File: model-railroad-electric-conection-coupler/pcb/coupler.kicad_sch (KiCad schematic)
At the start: 3 parts, among them J1 Conn_01x03_Pin, J2 Conn_01x06_Pin, J3 Conn_01x03_Pin

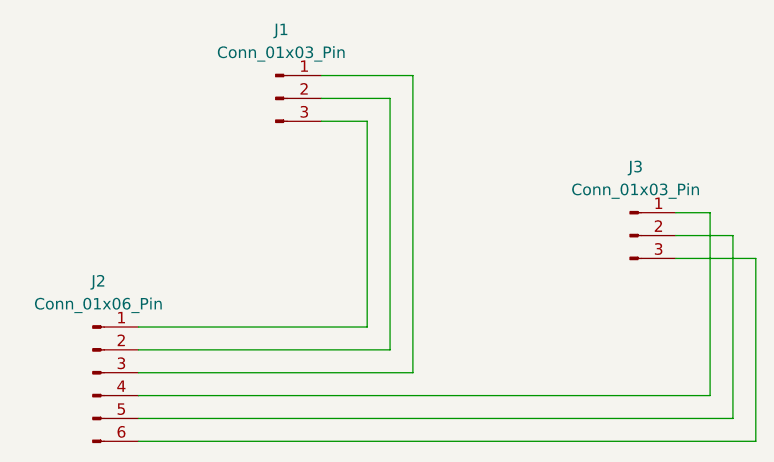
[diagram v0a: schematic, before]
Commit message: 鉄道模型用の通電カプラー PCB 版 v1
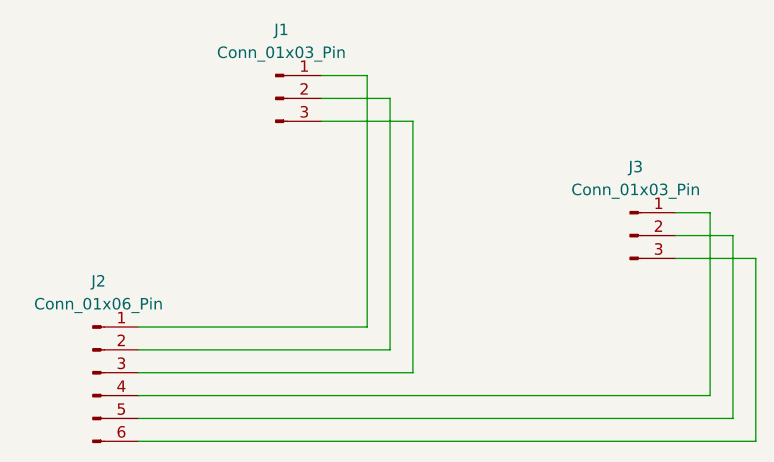
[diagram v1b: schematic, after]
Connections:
- net at J2.1 (Pin_1): now also J1.1 (Pin_1); no longer J1.3 (Pin_3)
- net at J2.3 (Pin_3): now also J1.3 (Pin_3); no longer J1.1 (Pin_1)
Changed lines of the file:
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@@
 	(wire
 		(pts
-			(xy 80.01 73.66) (xy 85.09 73.66)
+			(xy 85.09 96.52) (xy 85.09 68.58)
 		)
 		(stroke
@@
 	(wire
 		(pts
-			(xy 80.01 68.58) (xy 90.17 68.58)
+			(xy 85.09 68.58) (xy 80.01 68.58)
+		)
+		(stroke
+			(width 0)
+			(type default)
+		)
+	)
+	(wire
+		(pts
+			(xy 128.27 109.22) (xy 59.69 109.22)
+		)
+		(stroke
+			(width 0)
+			(type default)
+		)
+	)
+	(wire
+		(pts
+			(xy 87.63 71.12) (xy 87.63 99.06)
+		)
+		(stroke
+			(width 0)
+			(type default)
+		)
+	)
+	(wire
+		(pts
+			(xy 123.19 83.82) (xy 123.19 104.14)
+		)
+		(stroke
+			(width 0)
+			(type default)
+		)
+	)
+	(wire
+		(pts
+			(xy 90.17 73.66) (xy 90.17 101.6)
+		)
+		(stroke
+			(width 0)
+			(type default)
+		)
+	)
+	(wire
+		(pts
+			(xy 128.27 88.9) (xy 128.27 109.22)
 		)
 		(stroke
@@
 	(wire
 		(pts
-			(xy 128.27 109.22) (xy 59.69 109.22)
+			(xy 119.38 83.82) (xy 123.19 83.82)
 		)
 		(stroke
@@
 	(wire
 		(pts
-			(xy 123.19 83.82) (xy 123.19 104.14)
-		)
-		(stroke
-			(width 0)
-			(type default)
-		)
-	)
-	(wire
-		(pts
-			(xy 128.27 88.9) (xy 128.27 109.22)
-		)
-		(stroke
-			(width 0)
-			(type default)
-		)
-	)
-	(wire
-		(pts
-			(xy 90.17 68.58) (xy 90.17 101.6)
-		)
-		(stroke
-			(width 0)
-			(type default)
-		)
-	)
-	(wire
-		(pts
-			(xy 87.63 71.12) (xy 87.63 99.06)
-		)
-		(stroke
-			(width 0)
-			(type default)
-		)
-	)
-	(wire
-		(pts
-			(xy 119.38 83.82) (xy 123.19 83.82)
+			(xy 80.01 73.66) (xy 90.17 73.66)
 		)
 		(stroke
@@
 		)
 		(stroke
-			(width 0)
-			(type default)
-		)
-	)
-	(wire
-		(pts
-			(xy 85.09 73.66) (xy 85.09 96.52)
-		)
-		(stroke
